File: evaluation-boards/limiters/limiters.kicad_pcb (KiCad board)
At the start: 4 copper layers, 180 x 20 mm, 132 parts, among them J1 Conn_01x02, J10 Conn_Coaxial, J11 Conn_Coaxial, J12 Conn_Coaxial, J13 Conn_Coaxial, J14 Conn_Coaxial, J15 Conn_Coaxial, J16 Conn_Coaxial, J17 Conn_Coaxial, J18 Conn_Coaxial, J19 Conn_Coaxial, J2 Conn_01x02, J20 Conn_Coaxial, J21 Conn_Coaxial, J22 Conn_Coaxial, J23 Conn_Coaxial, J24 Conn_Coaxial, J25 Conn_Coaxial, J26 Conn_Coaxial, J27 Conn_Coaxial, J28 Conn_Coaxial, J29 Conn_Coaxial, J3 Conn_Coaxial, J30 Conn_Coaxial, J31 Conn_Coaxial, J32 Conn_Coaxial, J33 Conn_Coaxial, J34 Conn_Coaxial, J35 Conn_Coaxial, J36 Conn_Coaxial, J37 Conn_Coaxial, J38 Conn_Coaxial, J4 Conn_Coaxial, J5 Conn_Coaxial, J6 Conn_Coaxial, J7 Conn_Coaxial, J8 Conn_Coaxial, J9 Conn_Coaxial, U1 SKY13453

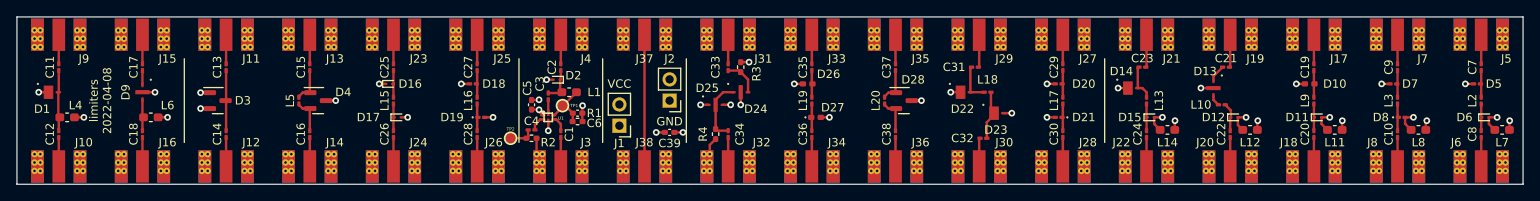
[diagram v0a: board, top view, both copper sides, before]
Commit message: Update RF test boards
- limiters
- rf-switch-spdt
- rf-switch-sp3t
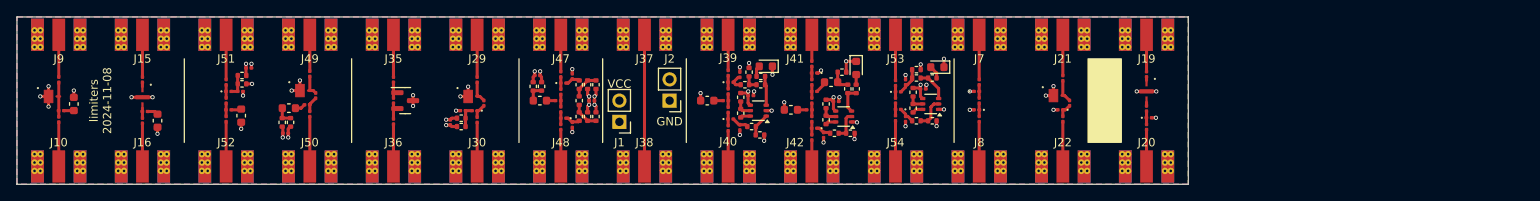
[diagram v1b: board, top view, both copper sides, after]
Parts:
- removed C14, C15, C16, C19, C20, C25, C26, C27, C28, C29, C30, C33, C34, C35, C36: 220 nF, Capacitor_SMD:C_0201_0603Metric_Pad0.64x0.40mm_HandSolder
- removed C39: 10 nF, Capacitor_SMD:C_0402_1005Metric_Pad0.74x0.62mm_HandSolder
- removed D10, D26, D27: D, Diode_SMD:D_0402_1005Metric_Pad0.77x0.64mm_HandSolder
- removed D11, D12, D15, D16, D17, D6: D_Schottky, Diode_SMD:D_SOD-923
- removed D18, D19: D_Schottky, Diode_SMD:D_0201_0603Metric_Pad0.64x0.40mm_HandSolder
- removed D20, D21: D, Diode_SMD:D_0201_0603Metric_Pad0.64x0.40mm_HandSolder
- removed D23: D, limiters:SMP1345-087LF
- removed D24, D25: D_AKA, limiters:SMP1304-085LF
- removed J11, J12, J13, J14, J17, J18, J23, J24, J25, J26, J27, J28, J3, J31, J32, J33, J34, J4, J5, J6: Conn_Coaxial, limiters:SMA-EDGE
- removed L11, L12, L14, L6, L7, L8: L, Inductor_SMD:L_0603_1608Metric_Pad1.05x0.95mm_HandSolder
- removed L15, L17, L19: 1.4 nH, Inductor_SMD:L_0201_0603Metric_Pad0.64x0.40mm_HandSolder
- removed L16: 1.0 nH, Inductor_SMD:L_0201_0603Metric_Pad0.64x0.40mm_HandSolder
- removed L9: 0.4 nH, Inductor_SMD:L_0201_0603Metric_Pad0.64x0.40mm_HandSolder
- removed R3, R4: 10k, Resistor_SMD:R_0402_1005Metric_Pad0.72x0.64mm_HandSolder
- removed TP1, TP2: TestPoint, gsg-modules:TESTPOINT-50MIL
- removed U1: SKY13453, gsg-modules:SKY13350-385LF
- added C40: 1 uF, Capacitor_SMD:C_0201_0603Metric, F.Cu at (130.0, 106.7)
- added C41: 1 uF, Capacitor_SMD:C_0201_0603Metric, F.Cu at (130.0, 113.3)
- added C42: 1 uF, Capacitor_SMD:C_0201_0603Metric, F.Cu at (131.4, 106.9)
- added C43: 1 uF, Capacitor_SMD:C_0201_0603Metric, F.Cu at (131.4, 113.2)
- added C44: 1 uF, Capacitor_SMD:C_0201_0603Metric, F.Cu at (140.0, 105.6)
- added C46: 1 uF, Capacitor_SMD:C_0201_0603Metric, F.Cu at (141.4, 114.1)
- added C47: 1 uF, Capacitor_SMD:C_0201_0603Metric, F.Cu at (140.0, 114.4)
- added C52: 1 uF, Capacitor_SMD:C_0201_0603Metric, F.Cu at (140.0, 110.0)
- added C63: 1 uF, Capacitor_SMD:C_0201_0603Metric, F.Cu at (110.0, 106.8)
- added C64: 1 uF, Capacitor_SMD:C_0201_0603Metric, F.Cu at (111.4, 107.1)
- added C65: 220 nF, Capacitor_SMD:C_0201_0603Metric, F.Cu at (80.0, 106.8)
- added C66: 220 nF, Capacitor_SMD:C_0201_0603Metric, F.Cu at (80.0, 111.6)
- added C67: 220 nF, Capacitor_SMD:C_0201_0603Metric, F.Cu at (70.0, 107.8)
- added C68: 1 uF, Capacitor_SMD:C_0201_0603Metric, F.Cu at (111.4, 112.9)
- added C69: 1 uF, Capacitor_SMD:C_0201_0603Metric, F.Cu at (110.0, 113.2)
- added C70: 220 nF, Capacitor_SMD:C_0201_0603Metric, F.Cu at (70.0, 112.2)
- added C71: 1 uF, Capacitor_SMD:C_0201_0603Metric, F.Cu at (71.7, 108.9)
- added C72: 1 uF, Capacitor_SMD:C_0201_0603Metric, F.Cu at (150.0, 107.9)
- added C73: 1 uF, Capacitor_SMD:C_0201_0603Metric, F.Cu at (151.2, 107.8)
- added C74: 1 uF, Capacitor_SMD:C_0201_0603Metric, F.Cu at (151.2, 112.2)
- added C75: 1 uF, Capacitor_SMD:C_0201_0603Metric, F.Cu at (150.0, 112.1)
- added D29: PIN, Diode_SMD:D_0201_0603Metric, F.Cu at (130.3, 107.8)
- added D30: Schottky, Diode_SMD:D_0201_0603Metric, F.Cu at (130.3, 112.2)
- added D31: PIN, Diode_SMD:D_0201_0603Metric, F.Cu at (140.3, 106.7)
- added D32: Schottky, Diode_SMD:D_0201_0603Metric, F.Cu at (140.3, 113.3)
- added D33: LED, LED_SMD:LED_0603_1608Metric, F.Cu at (134.5, 105.9)
- added D34: LED, LED_SMD:LED_0603_1608Metric, F.Cu at (145.3, 106.1)
- added D35: LED, LED_SMD:LED_0603_1608Metric, F.Cu at (155.0, 106.0)
- added D37: PIN, Diode_SMD:D_0201_0603Metric, F.Cu at (110.3, 107.9)
- added D38: Schottky, Diode_SMD:D_0201_0603Metric, F.Cu at (110.3, 112.1)
- added D39: PIN, limiters:SMP1345-087LF, F.Cu at (79.0, 108.8)
- added D41: PIN, Diode_SMD:D_0201_0603Metric, F.Cu at (150.3, 109.0)
- added D42: Schottky, Diode_SMD:D_0201_0603Metric, F.Cu at (150.3, 111.0)
- added J39: Conn_Coaxial, sma-variants:Linx_SMA_CONSMA003.062, F.Cu at (130.0, 100.0)
- added J40: Conn_Coaxial, sma-variants:Linx_SMA_CONSMA003.062, F.Cu at (130.0, 120.0)
- added J41: Conn_Coaxial, sma-variants:Linx_SMA_CONSMA003.062, F.Cu at (140.0, 100.0)
- added J42: Conn_Coaxial, sma-variants:Linx_SMA_CONSMA003.062, F.Cu at (140.0, 120.0)
- added J47: Conn_Coaxial, sma-variants:Linx_SMA_CONSMA003.062, F.Cu at (110.0, 100.0)
- added J48: Conn_Coaxial, sma-variants:Linx_SMA_CONSMA003.062, F.Cu at (110.0, 120.0)
- added J49: Conn_Coaxial, sma-variants:Linx_SMA_CONSMA003.062, F.Cu at (80.0, 100.0)
- added J50: Conn_Coaxial, sma-variants:Linx_SMA_CONSMA003.062, F.Cu at (80.0, 120.0)
- added J51: Conn_Coaxial, sma-variants:Linx_SMA_CONSMA003.062, F.Cu at (70.0, 100.0)
- added J52: Conn_Coaxial, sma-variants:Linx_SMA_CONSMA003.062, F.Cu at (70.0, 120.0)
- added J53: Conn_Coaxial, sma-variants:Linx_SMA_CONSMA003.062, F.Cu at (150.0, 100.0)
- added J54: Conn_Coaxial, sma-variants:Linx_SMA_CONSMA003.062, F.Cu at (150.0, 120.0)
- added L21: 0.5 nH, Inductor_SMD:L_0201_0603Metric, F.Cu at (130.0, 111.1)
- added L22: 47uH, Inductor_SMD:L_0603_1608Metric, F.Cu at (127.5, 110.0)
- added L23: 33nH, Inductor_SMD:L_0201_0603Metric, F.Cu at (129.7, 110.0)
- added L24: 0.5 nH, Inductor_SMD:L_0201_0603Metric, F.Cu at (130.0, 108.9)
- added L25: 0.5 nH, Inductor_SMD:L_0201_0603Metric, F.Cu at (140.0, 107.8)
- added L26: 47uH, Inductor_SMD:L_0603_1608Metric, F.Cu at (137.5, 111.1)
- added L27: 33nH, Inductor_SMD:L_0201_0603Metric, F.Cu at (139.7, 111.1)
- added L28: 0.5 nH, Inductor_SMD:L_0201_0603Metric, F.Cu at (140.0, 112.2)
- added L29: 47uH, Inductor_SMD:L_0603_1608Metric, F.Cu at (142.3, 107.8)
- added L30: 33nH, Inductor_SMD:L_0201_0603Metric, F.Cu at (140.3, 108.9)
- added L35: 0.5 nH, Inductor_SMD:L_0201_0603Metric, F.Cu at (110.0, 109.0)
- added L37: 47uH, Inductor_SMD:L_0603_1608Metric, F.Cu at (107.5, 110.0)
- added L38: 33nH, Inductor_SMD:L_0201_0603Metric, F.Cu at (109.7, 110.0)
- added L39: 0.5 nH, Inductor_SMD:L_0201_0603Metric, F.Cu at (110.0, 111.0)
- added L40: 0.5 nH, Inductor_SMD:L_0201_0603Metric, F.Cu at (70.0, 110.0)
- added L41: 47uH, Inductor_SMD:L_0603_1608Metric, F.Cu at (77.5, 110.9)
- added L42: 33nH, Inductor_SMD:L_0201_0603Metric, F.Cu at (79.7, 110.5)
- added L43: 0.5 nH, Inductor_SMD:L_0201_0603Metric, F.Cu at (80.7, 109.4)
- added L44: 47uH, Inductor_SMD:L_0603_1608Metric, F.Cu at (71.8, 111.8)
- added L45: 33nH, Inductor_SMD:L_0201_0603Metric, F.Cu at (70.3, 111.1)
- added L46: 1 nH, Inductor_SMD:L_0201_0603Metric, F.Cu at (150.0, 110.0)
- added Q1: NPN+PNP, Package_TO_SOT_SMD:SOT-363_SC-70-6, F.Cu at (133.6, 111.2)
- added Q2: NPN+PNP, Package_TO_SOT_SMD:SOT-363_SC-70-6, F.Cu at (143.8, 111.9)
- added Q3: NPN+PNP, Package_TO_SOT_SMD:SOT-363_SC-70-6, F.Cu at (154.2, 110.4)
- added R10: 1k, Resistor_SMD:R_0402_1005Metric, F.Cu at (133.9, 108.1)
- added R11: 0, Resistor_SMD:R_0402_1005Metric, F.Cu at (132.0, 108.1)
- added R12: 1k, Resistor_SMD:R_0402_1005Metric, F.Cu at (133.9, 107.1)
- added R13: 10k, Resistor_SMD:R_0402_1005Metric, F.Cu at (143.6, 106.6)
- added R14: 1k, Resistor_SMD:R_0402_1005Metric, F.Cu at (144.3, 108.6)
- added R15: 10k, Resistor_SMD:R_0402_1005Metric, F.Cu at (141.7, 110.4)
- added R16: 1k, Resistor_SMD:R_0402_1005Metric, F.Cu at (141.7, 112.3)
- added R17: 1k, Resistor_SMD:R_0402_1005Metric, F.Cu at (142.7, 113.9)
- added R18: 10k, Resistor_SMD:R_0402_1005Metric, F.Cu at (144.6, 113.9)
- added R19: 1k, Resistor_SMD:R_0402_1005Metric, F.Cu at (145.3, 108.6)
- added R20: 1k, Resistor_SMD:R_0402_1005Metric, F.Cu at (154.4, 107.3)
- added R36: 10k, Resistor_SMD:R_0402_1005Metric, F.Cu at (113.2, 111.9)
- added R37: 10k, Resistor_SMD:R_0402_1005Metric, F.Cu at (114.2, 111.9)
- added R38: 0, Resistor_SMD:R_0402_1005Metric, F.Cu at (112.2, 111.9)
- added R39: 0, Resistor_SMD:R_0402_1005Metric, F.Cu at (112.2, 108.1)
- added R40: 1k, Resistor_SMD:R_0402_1005Metric, F.Cu at (76.7, 112.6)
- added R41: 10k, Resistor_SMD:R_0402_1005Metric, F.Cu at (77.7, 112.6)
- added R42: 1k, Resistor_SMD:R_0402_1005Metric, F.Cu at (71.9, 108.0)
- added R43: 10k, Resistor_SMD:R_0402_1005Metric, F.Cu at (71.9, 107.0)
- added R44: 1k, Resistor_SMD:R_0402_1005Metric, F.Cu at (106.7, 108.3)
- added R45: 10k, Resistor_SMD:R_0402_1005Metric, F.Cu at (107.7, 108.3)
- added R46: 10k, Resistor_SMD:R_0402_1005Metric, F.Cu at (114.2, 108.1)
- added R47: 10k, Resistor_SMD:R_0402_1005Metric, F.Cu at (113.2, 108.1)
- added R48: 0, Resistor_SMD:R_0402_1005Metric, F.Cu at (112.2, 110.0)
- added R49: 1k, Resistor_SMD:R_0402_1005Metric, F.Cu at (152.5, 106.3)
- added R5: 10k, Resistor_SMD:R_0402_1005Metric, F.Cu at (133.8, 114.1)
- added R50: 3.3k, Resistor_SMD:R_0402_1005Metric, F.Cu at (152.5, 107.3)
- added R51: 10k, Resistor_SMD:R_0402_1005Metric, F.Cu at (152.1, 109.0)
- added R52: 1k, Resistor_SMD:R_0402_1005Metric, F.Cu at (152.1, 110.9)
- added R53: 1k, Resistor_SMD:R_0402_1005Metric, F.Cu at (152.5, 112.4)
- added R54: 10k, Resistor_SMD:R_0402_1005Metric, F.Cu at (154.4, 112.4)
- added R6: 10k, Resistor_SMD:R_0402_1005Metric, F.Cu at (131.5, 109.6)
- added R7: 1k, Resistor_SMD:R_0402_1005Metric, F.Cu at (132.8, 113.1)
- added R8: 1k, Resistor_SMD:R_0402_1005Metric, F.Cu at (131.5, 111.5)
- added R9: 10k, Resistor_SMD:R_0402_1005Metric, F.Cu at (132.5, 106.6)
- C1, C13, C2, C3, C4, C7, C8: value 220 nF -> 1 uF; footprint Capacitor_SMD:C_0201_0603Metric_Pad0.64x0.40mm_HandSolder -> Capacitor_SMD:C_0201_0603Metric
- C10, C11, C12, C17, C18, C21, C22, C23, C24, C31, C32, C37, C38, C9: footprint Capacitor_SMD:C_0201_0603Metric_Pad0.64x0.40mm_HandSolder -> Capacitor_SMD:C_0201_0603Metric
- C5: value 10 nF -> 1 uF; footprint Capacitor_SMD:C_0402_1005Metric_Pad0.74x0.62mm_HandSolder -> Capacitor_SMD:C_0201_0603Metric
- C6: value C -> 1 uF; footprint Capacitor_SMD:C_0402_1005Metric_Pad0.74x0.62mm_HandSolder -> Capacitor_SMD:C_0201_0603Metric
- D1, D14, D22: value D -> PIN
- D13, D9: value D_AKA -> PIN
- D2: value D_Schottky -> Schottky; footprint Diode_SMD:D_SOD-923 -> Diode_SMD:D_0201_0603Metric
- D28: value D_Dual_Series_AKC -> Dual_PIN
- D3: value D_Schottky_Dual_Series_AKC -> Schottky; footprint Package_TO_SOT_SMD:SOT-23 -> Diode_SMD:D_0201_0603Metric
- D4: value D_Schottky_Dual_Series_AKC -> PIN; footprint Package_TO_SOT_SMD:SOT-23 -> Diode_SMD:D_0201_0603Metric
- D5, D7: value D -> PIN; footprint Diode_SMD:D_0201_0603Metric_Pad0.64x0.40mm_HandSolder -> Diode_SMD:D_0201_0603Metric
- D8: value D_Schottky -> Schottky; footprint Diode_SMD:D_0201_0603Metric_Pad0.64x0.40mm_HandSolder -> Diode_SMD:D_0201_0603Metric
- J10, J15, J16, J19, J20, J21, J22, J29, J30, J35, J36, J37, J38, J7, J8, J9: footprint limiters:SMA-EDGE -> sma-variants:Linx_SMA_CONSMA003.062
- L1, L4: value L -> 33nH; footprint Inductor_SMD:L_0603_1608Metric_Pad1.05x0.95mm_HandSolder -> Inductor_SMD:L_0201_0603Metric
- L10, L18, L20, L3: footprint Inductor_SMD:L_0201_0603Metric_Pad0.64x0.40mm_HandSolder -> Inductor_SMD:L_0201_0603Metric
- L13: value 0.4 nH -> 0.5 nH; footprint Inductor_SMD:L_0201_0603Metric_Pad0.64x0.40mm_HandSolder -> Inductor_SMD:L_0201_0603Metric
- L2: value 0.4 nH -> 47uH; footprint Inductor_SMD:L_0201_0603Metric_Pad0.64x0.40mm_HandSolder -> Inductor_SMD:L_0603_1608Metric
- L5: value 1.4 nH -> 47uH; footprint Inductor_SMD:L_0201_0603Metric_Pad0.64x0.40mm_HandSolder -> Inductor_SMD:L_0603_1608Metric
- R1: value 10k -> 1k; footprint Resistor_SMD:R_0402_1005Metric_Pad0.72x0.64mm_HandSolder -> Resistor_SMD:R_0402_1005Metric
- R2: value 50 -> 10k; footprint Resistor_SMD:R_0402_1005Metric_Pad0.72x0.64mm_HandSolder -> Resistor_SMD:R_0402_1005Metric
- moved L2 168.2 mm to (51.8, 110.4)
- moved D5 149.2 mm to (70.3, 108.9)
- moved D3 100.7 mm to (169.7, 111.1), turned to 180 degrees
- moved C7 87.4 mm to (132.7, 109.4), turned to 0 degrees
- moved C8 77.2 mm to (142.9, 110.1), turned to 0 degrees
- moved D2 70.9 mm to (180.3, 112.0), turned to 0 degrees
- moved L1 60.7 mm to (50.3, 111.2), turned to 0 degrees
- moved C32 60.5 mm to (100.0, 112.3), turned to 90 degrees
- moved L18 60.2 mm to (100.8, 110.3), turned to 90 degrees
- moved C37 60.0 mm to (90.0, 107.5)
- moved C38 60.0 mm to (90.0, 112.5)
- moved J29 60.0 mm to (100.0, 100.0)
- moved J30 60.0 mm to (100.0, 120.0)
- moved J35 60.0 mm to (90.0, 100.0)
- moved J36 60.0 mm to (90.0, 120.0)
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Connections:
- C1 pad 1: Net-(C1-Pad1) -> Net-(D4-A)
- C1 pad 2: Net-(C1-Pad2) -> GND
- C11 pad 1: Net-(C11-Pad1) -> Net-(D1-A)
- C12 pad 2: Net-(C11-Pad1) -> Net-(D1-A)
- C13 pad 1: Net-(C13-Pad1) -> VCC
- C13 pad 2: Net-(C13-Pad2) -> GND
- C2 pad 1: Net-(C2-Pad1) -> VCC
- C2 pad 2: Net-(C2-Pad2) -> GND
- C22 pad 2: Net-(C22-Pad2) -> Net-(D2-K)
- C24 pad 2: Net-(C24-Pad2) -> Net-(D3-K)
- C3 pad 1: Net-(C3-Pad1) -> VCC
- C3 pad 2: Net-(C2-Pad1) -> GND
- C32 pad 2: Net-(C32-Pad2) -> Net-(D4-K)
- C4 pad 1: Net-(C4-Pad1) -> VCC
- C4 pad 2: Net-(C4-Pad2) -> GND
- C5 pad 1: GND -> VCC
- C5 pad 2: VCC -> GND
- C6 pad 1: Net-(C6-Pad1) -> VCC
- C7 pad 1: Net-(C7-Pad1) -> VCC
- C7 pad 2: Net-(C7-Pad2) -> GND
- C8 pad 1: Net-(C8-Pad1) -> VCC
- C8 pad 2: Net-(C8-Pad2) -> GND
- D1 pad 2: Net-(C11-Pad1) -> Net-(D1-A)
- D2 pad 1: Net-(C2-Pad1) -> Net-(D2-K)
- D3 pad 1: GND -> Net-(D3-K)
- D4 pad 1: Net-(C15-Pad1) -> Net-(D4-K)
- D4 pad 2: Net-(C16-Pad2) -> Net-(D4-A)
- D5 pad 1: GND -> Net-(D5-K)
- D5 pad 2: Net-(C7-Pad1) -> Net-(D5-A)
- L1 pad 1: Net-(C6-Pad1) -> Net-(D1-A)
- L1 pad 2: Net-(C2-Pad1) -> Net-(L1-Pad2)
- L10 pad 1: Net-(C22-Pad2) -> Net-(D2-K)
- L13 pad 1: Net-(C24-Pad2) -> Net-(D3-K)
- L18 pad 1: Net-(C32-Pad2) -> Net-(D4-K)
- L2 pad 1: Net-(C8-Pad2) -> Net-(L1-Pad2)
- L2 pad 2: Net-(C7-Pad1) -> GND
- L4 pad 1: Net-(C11-Pad1) -> Net-(C18-Pad2)
- L4 pad 2: GND -> Net-(L4-Pad2)
- L5 pad 1: Net-(C16-Pad2) -> Net-(L4-Pad2)
- L5 pad 2: Net-(C15-Pad1) -> GND
- R1 pad 1: Net-(C6-Pad1) -> Net-(D4-A)
- R2 pad 1: Net-(C4-Pad1) -> Net-(D4-A)
- R2 pad 2: GND -> VCC
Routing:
- net VCC: track 5.31 -> 16.7 mm, vias 4 -> 9
- net GND: track 55.6 -> 47.1 mm, vias 40 -> 55
- net Net-(C34-Pad2): track 7.58 -> 0.00 mm
- net Net-(C11-Pad1): track 7.33 -> 0.00 mm
- net Net-(C13-Pad1): track 7.19 -> 0.00 mm
- net Net-(C6-Pad1): track 6.58 -> 0.00 mm
- net Net-(C32-Pad2): track 6.01 -> 0.00 mm
- net Net-(J50-In): track 0.00 -> 5.95 mm
- net Net-(J54-In): track 0.00 -> 5.45 mm
- net Net-(J53-In): track 0.00 -> 5.45 mm
- net Net-(J52-In): track 0.00 -> 5.35 mm
- net Net-(J51-In): track 0.00 -> 5.35 mm
- net Net-(J48-In): track 0.00 -> 4.40 mm
- net Net-(J47-In): track 0.00 -> 4.40 mm
- net Net-(C2-Pad1): track 4.37 -> 0.00 mm
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- added copper zone on B.Cu, net GND
- added copper zone on F.Cu, net GND
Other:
- board size 180 x 20 mm -> 140 x 20 mm
- board text added: "limiters 2024-11-08"
- board text removed: "limiters 2022-04-08"

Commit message: Update limiters board
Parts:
- removed C37, C38, C65, C66: 220 nF, Capacitor_SMD:C_0201_0603Metric
- removed C40, C41, C42, C43, C44, C46, C47, C52, C72, C73, C74, C75: 1 uF, Capacitor_SMD:C_0201_0603Metric
- removed D22, D39: PIN, limiters:SMP1345-087LF
- removed D28: Dual_PIN, Package_TO_SOT_SMD:SOT-23
- removed D29, D31, D41: PIN, Diode_SMD:D_0201_0603Metric
- removed D30, D32, D42: Schottky, Diode_SMD:D_0201_0603Metric
- removed D33, D34, D35: LED, LED_SMD:LED_0603_1608Metric
- removed J20, J21, J22, J29, J30, J35, J36, J39, J40, J41, J42, J49, J50, J53, J54: Conn_Coaxial, sma-variants:Linx_SMA_CONSMA003.062
- removed L10: 0.6 nH, Inductor_SMD:L_0201_0603Metric
- removed L13, L21, L24, L25, L28, L35, L39, L40, L43: 0.5 nH, Inductor_SMD:L_0201_0603Metric
- removed L18: 0.8 nH, Inductor_SMD:L_0201_0603Metric
- removed L20: 1.4 nH, Inductor_SMD:L_0201_0603Metric
- removed L22, L26, L29, L37, L41, L44: 47uH, Inductor_SMD:L_0603_1608Metric
- removed L23, L27, L30, L38, L42, L45: 33nH, Inductor_SMD:L_0201_0603Metric
- removed L46: 1 nH, Inductor_SMD:L_0201_0603Metric
- removed Q3: NPN+PNP, Package_TO_SOT_SMD:SOT-363_SC-70-6
- removed R18, R45, R51, R54: 10k, Resistor_SMD:R_0402_1005Metric
- removed R19, R20, R44, R49, R52, R53: 1k, Resistor_SMD:R_0402_1005Metric
- removed R50: 3.3k, Resistor_SMD:R_0402_1005Metric
- added C14: C, Capacitor_SMD:C_0201_0603Metric, F.Cu at (87.2, 109.5)
- added C15: 1 uF, Capacitor_SMD:C_0201_0603Metric, F.Cu at (138.4, 111.2)
- added C16: 1 uF, Capacitor_SMD:C_0402_1005Metric, F.Cu at (100.0, 108.6)
- added C19: 1 uF, Capacitor_SMD:C_0201_0603Metric, F.Cu at (130.0, 113.0)
- added C20: 1 uF, Capacitor_SMD:C_0201_0603Metric, F.Cu at (128.6, 110.7)
- added C25: C, Capacitor_SMD:C_0201_0603Metric, F.Cu at (122.9, 108.6)
- added C26: C, Capacitor_SMD:C_0201_0603Metric, F.Cu at (125.3, 106.4)
- added C27: 1 uF, Capacitor_SMD:C_0201_0603Metric, F.Cu at (126.7, 106.4)
- added C28: 1 uF, Capacitor_SMD:C_0201_0603Metric, F.Cu at (122.9, 107.2)
- added C29: 1 uF, Capacitor_SMD:C_0201_0603Metric, F.Cu at (148.3, 111.0)
- added C30: 1 uF, Capacitor_SMD:C_0201_0603Metric, F.Cu at (150.0, 110.6)
- added C33: 1 uF, Capacitor_SMD:C_0201_0603Metric, F.Cu at (160.0, 110.7)
- added C34: 1 uF, Capacitor_SMD:C_0201_0603Metric, F.Cu at (143.7, 113.4)
- added C35: 1 uF, Capacitor_SMD:C_0201_0603Metric, F.Cu at (153.8, 113.4)
- added D10: PIN, eval:TSLP-2-19, F.Cu at (148.9, 109.5)
- added D11: Schottky, eval:TSSLP-2-1, F.Cu at (149.2, 110.2)
- added D12: PIN, eval:TSLP-2-19, F.Cu at (158.9, 109.1)
- added D6: Schottky, eval:TSSLP-2-1, F.Cu at (100.8, 109.8)
- added J11: Conn_Coaxial, sma-variants:Linx_SMA_CONSMA003.062, F.Cu at (100.0, 120.0)
- added J12: Conn_Coaxial, sma-variants:Linx_SMA_CONSMA003.062, F.Cu at (130.0, 100.0)
- added J13: Conn_Coaxial, sma-variants:Linx_SMA_CONSMA003.062, F.Cu at (130.0, 120.0)
- added J14: Conn_Coaxial, sma-variants:Linx_SMA_CONSMA003.062, F.Cu at (150.0, 100.0)
- added J17: Conn_Coaxial, sma-variants:Linx_SMA_CONSMA003.062, F.Cu at (160.0, 100.0)
- added J18: Conn_Coaxial, sma-variants:Linx_SMA_CONSMA003.062, F.Cu at (160.0, 120.0)
- added J3: Conn_Coaxial, sma-variants:Linx_SMA_CONSMA003.062, F.Cu at (110.0, 100.0)
- added J4: Conn_Coaxial, sma-variants:Linx_SMA_CONSMA003.062, F.Cu at (110.0, 120.0)
- added J5: Conn_Coaxial, sma-variants:Linx_SMA_CONSMA003.062, F.Cu at (140.0, 100.0)
- added J6: Conn_Coaxial, sma-variants:Linx_SMA_CONSMA003.062, F.Cu at (140.0, 120.0)
- added L6: 1.0 nH, Inductor_SMD:L_0201_0603Metric, F.Cu at (130.0, 110.0)
- added L7: L, Inductor_SMD:L_0805_2012Metric, F.Cu at (76.9, 111.2)
- added L8: L, Inductor_SMD:L_0201_0603Metric, F.Cu at (78.3, 110.0)
- added L9: L, Inductor_SMD:L_0201_0603Metric, F.Cu at (79.7, 110.0)
- added Q4: NMOS/PMOS, Package_TO_SOT_SMD:SOT-563, F.Cu at (134.6, 111.7)
- added R21: R, Resistor_SMD:R_0201_0603Metric, F.Cu at (86.8, 110.6)
- added R22: R, Resistor_SMD:R_0201_0603Metric, F.Cu at (87.2, 108.2)
- added R23: 10k, Resistor_SMD:R_0402_1005Metric, F.Cu at (135.1, 109.8)
- added R24: 10k, Resistor_SMD:R_0402_1005Metric, F.Cu at (136.7, 113.1)
- added R25: 10k, Resistor_SMD:R_0402_1005Metric, F.Cu at (127.7, 110.9)
- added R27: 10k, Resistor_SMD:R_0402_1005Metric, F.Cu at (128.0, 106.6)
- added R28: 10k, Resistor_SMD:R_0402_1005Metric, F.Cu at (125.9, 114.2)
- added R29: 10k, Resistor_SMD:R_0402_1005Metric, F.Cu at (126.9, 114.2)
- added R3: R, Resistor_SMD:R_0201_0603Metric, F.Cu at (86.5, 109.5)
- added R30: 10k, Resistor_SMD:R_0402_1005Metric, F.Cu at (122.3, 112.6)
- added R31: 10k, Resistor_SMD:R_0402_1005Metric, F.Cu at (122.0, 108.4)
- added R32: 10k, Resistor_SMD:R_0402_1005Metric, F.Cu at (124.1, 114.2)
- added R33: 3.3k, Resistor_SMD:R_0402_1005Metric, F.Cu at (122.3, 114.2)
- added R34: 10k, Resistor_SMD:R_0402_1005Metric, F.Cu at (121.3, 114.2)
- added R35: 0, Resistor_SMD:R_0402_1005Metric, F.Cu at (122.3, 110.8)
- added R4: R, Resistor_SMD:R_0201_0603Metric, F.Cu at (88.2, 109.9)
- added R55: 10k, Resistor_SMD:R_0402_1005Metric, F.Cu at (122.3, 109.8)
- added R56: 10k, Resistor_SMD:R_0402_1005Metric, F.Cu at (127.3, 108.5)
- added R57: 10k, Resistor_SMD:R_0402_1005Metric, F.Cu at (125.8, 105.1)
- added R58: 3.3k, Resistor_SMD:R_0402_1005Metric, F.Cu at (124.8, 105.1)
- added U1: MADL-011021-14150T, eval:TDFN-6-1EP_1.5x1.2mm_P0.4mm_EP0.47x0.8mm, F.Cu at (110.0, 110.0)
- added U2: LMV358, Package_SO:MSOP-8_3x3mm_P0.65mm, F.Cu at (125.0, 110.0)
- C10, C12, C17, C18, C21, C24, C32, C67, C70: value 220 nF -> 1 uF
- C11, C22, C23: value 220 nF -> C
- C31, C9: value 220 nF -> 1 uF; footprint Capacitor_SMD:C_0201_0603Metric -> Capacitor_SMD:C_0402_1005Metric
- C4, C8: footprint Capacitor_SMD:C_0201_0603Metric -> Capacitor_SMD:C_0402_1005Metric
- C6, C7: value 1 uF -> C
- D1, D14: footprint limiters:SMP1345-087LF -> eval:TSLP-2-19
- D13, D9: value PIN -> Schottky; footprint limiters:SMP1304-085LF -> eval:TSSLP-2-1
- D2, D38, D8: footprint Diode_SMD:D_0201_0603Metric -> eval:TSSLP-2-1
- D3: value Schottky -> PIN; footprint Diode_SMD:D_0201_0603Metric -> eval:TSLP-2-19
- D37, D4, D5, D7: footprint Diode_SMD:D_0201_0603Metric -> eval:TSLP-2-19
- J16, J19, J9: value Conn_Coaxial -> Conn_01x02; footprint sma-variants:Linx_SMA_CONSMA003.062 -> Connector_PinHeader_2.54mm:PinHeader_1x02_P2.54mm_Vertical
- L1: value 33nH -> L
- L2: value 47uH -> L; footprint Inductor_SMD:L_0603_1608Metric -> Inductor_SMD:L_0201_0603Metric
- L4: value 33nH -> L; footprint Inductor_SMD:L_0201_0603Metric -> Inductor_SMD:L_0805_2012Metric
- L5: value 47uH -> 1.0 nH; footprint Inductor_SMD:L_0603_1608Metric -> Inductor_SMD:L_0201_0603Metric
- Q1, Q2: value NPN+PNP -> NMOS/PMOS; footprint Package_TO_SOT_SMD:SOT-363_SC-70-6 -> Package_TO_SOT_SMD:SOT-563
- R12, R16, R40: value 1k -> 10k
- R15, R2, R41: value 10k -> 0
- R17, R7, R8: value 1k -> R; footprint Resistor_SMD:R_0402_1005Metric -> Resistor_SMD:R_0201_0603Metric
- R42: value 1k -> 0
- R5, R6: value 10k -> R; footprint Resistor_SMD:R_0402_1005Metric -> Resistor_SMD:R_0201_0603Metric
- moved J15 92.2 mm to (150.0, 120.0), turned to 90 degrees
- moved D7 90.7 mm to (69.0, 109.8)
- moved D8 90.5 mm to (69.2, 110.5)
- moved C9 90.0 mm to (70.0, 108.4)
- moved C12 90.0 mm to (140.0, 111.4)
- moved C10 90.0 mm to (70.0, 111.4)
- moved D1 90.0 mm to (139.0, 109.8), turned to 180 degrees
- moved J7 90.0 mm to (70.0, 100.0)
- moved J8 90.0 mm to (70.0, 120.0)
- moved L3 90.0 mm to (70.0, 110.0)
- moved J16 86.7 mm to (145.8, 107.5), turned to -90 degrees
- moved J9 86.6 mm to (136.3, 107.5)
- moved L5 78.2 mm to (140.0, 110.0), turned to 90 degrees
- moved C6 76.1 mm to (77.2, 109.0), turned to -90 degrees
- moved C18 70.2 mm to (130.0, 107.0)
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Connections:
- C1 pad 1: Net-(D4-A) -> Net-(U1-RFIN)
- C1 pad 2: GND -> Net-(J3-In)
- C11 pad 1: Net-(D1-A) -> GND
- C11 pad 2: Net-(J9-In) -> Net-(C11-Pad2)
- C12 pad 1: Net-(J10-In) -> Net-(J6-In)
- C12 pad 2: Net-(D1-A) -> Net-(D2-A)
- C17 pad 1: Net-(C17-Pad1) -> Net-(J11-In)
- C17 pad 2: Net-(J15-In) -> Net-(D4-A)
- C18 pad 1: Net-(J16-In) -> Net-(D3-K)
- C18 pad 2: Net-(C18-Pad2) -> Net-(J12-In)
- C21 pad 1: Net-(C21-Pad1) -> Net-(D3-A)
- C21 pad 2: Net-(J19-In) -> GND
- C22 pad 1: Net-(J20-In) -> Net-(C22-Pad1)
- C22 pad 2: Net-(D2-K) -> Net-(U2A--)
- C23 pad 1: Net-(D14-A) -> Net-(C22-Pad1)
- C23 pad 2: Net-(J21-In) -> Net-(U2A-+)
- C24 pad 1: Net-(J22-In) -> Net-(U2A-+)
- C24 pad 2: Net-(D3-K) -> GND
- C3 pad 1: VCC -> Net-(J4-In)
- C3 pad 2: GND -> Net-(U1-RFOUT)
- C31 pad 1: Net-(D22-A) -> Net-(D12-K)
- C32 pad 1: Net-(J30-In) -> Net-(D13-K)
- C32 pad 2: Net-(D4-K) -> GND
- C4 pad 1: VCC -> Net-(D1-K)
- C4 pad 2: GND -> Net-(J5-In)
- C6 pad 1: VCC -> Net-(C6-Pad1)
- C6 pad 2: GND -> Net-(C6-Pad2)
- C67 pad 1: Net-(D5-K) -> Net-(D5-A)
- C69 pad 2: Net-(D38-A) -> Net-(D37-K)
- C7 pad 1: VCC -> GND
- C7 pad 2: GND -> Net-(C7-Pad2)
- C70 pad 2: Net-(C70-Pad2) -> Net-(D5-A)
- C71 pad 1: Net-(D5-A) -> Net-(D5-K)
- C8 pad 1: VCC -> Net-(D10-K)
- C8 pad 2: GND -> Net-(J14-In)
- D1 pad 1: GND -> Net-(D1-K)
- D1 pad 2: Net-(D1-A) -> GND
- D13 pad 1: Net-(C21-Pad1) -> Net-(D13-K)
- D13 pad 2: GND -> Net-(D12-K)
- D14 pad 2: Net-(D14-A) -> Net-(D12-K)
- D2 pad 2: GND -> Net-(D2-A)
- D3 pad 2: GND -> Net-(D3-A)
- D38 pad 2: Net-(D38-A) -> Net-(D37-K)
- D4 pad 1: Net-(D4-K) -> GND
- D9 pad 1: Net-(C17-Pad1) -> Net-(D9-K)
- D9 pad 2: GND -> Net-(D9-A)
- J16 pad 1: Net-(J16-In) -> Net-(J16-Pin_1)
- J16 pad 2: GND -> Net-(J16-Pin_1)
- J19 pad 1: Net-(J19-In) -> Net-(J19-Pin_1)
- J19 pad 2: GND -> Net-(J19-Pin_1)
- J9 pad 1: Net-(J9-In) -> Net-(J9-Pin_1)
- J9 pad 2: GND -> Net-(J9-Pin_1)
- L1 pad 1: Net-(D1-A) -> Net-(D5-A)
- L2 pad 2: GND -> Net-(C14-Pad2)
- L4 pad 1: Net-(C18-Pad2) -> Net-(C14-Pad2)
- L5 pad 1: Net-(L4-Pad2) -> Net-(D2-A)
- L5 pad 2: GND -> Net-(D1-K)
- Q1 pad 1: Net-(Q1A-E1) -> GND
- Q1 pad 2: GND -> Net-(J16-Pin_1)
- Q1 pad 3: Net-(Q1B-C2) -> Net-(Q1B-D)
- Q1 pad 5: Net-(Q1B-B2) -> Net-(J16-Pin_1)
- Q1 pad 6: Net-(Q1A-C1) -> Net-(Q1A-D)
- Q2 pad 2: Net-(Q2A-B1) -> Net-(J19-Pin_1)
- Q2 pad 5: Net-(Q2B-B2) -> Net-(J19-Pin_1)
- Q2 pad 6: Net-(Q2A-C1) -> Net-(Q2A-D)
- R1 pad 1: Net-(D4-A) -> Net-(D2-K)
- R1 pad 2: GND -> Net-(Q4B-D)
- R10 pad 1: Net-(R10-Pad1) -> Net-(D11-K)
- R10 pad 2: Net-(Q1B-C2) -> Net-(Q1B-D)
- R11 pad 1: Net-(D29-A) -> Net-(D11-K)
- R11 pad 2: Net-(R10-Pad1) -> Net-(Q1A-D)
- R12 pad 1: Net-(D33-A) -> Net-(J16-Pin_1)
- R12 pad 2: Net-(Q1B-C2) -> GND
- R13 pad 1: Net-(L29-Pad2) -> Net-(D13-K)
- R14 pad 1: Net-(L29-Pad2) -> Net-(D13-K)
- R15 pad 1: VCC -> Net-(D13-K)
- R15 pad 2: Net-(Q2B-B2) -> Net-(Q2A-D)
- R16 pad 1: Net-(Q2B-B2) -> Net-(J19-Pin_1)
- R16 pad 2: Net-(Q2A-C1) -> GND
- R17 pad 1: Net-(D32-K) -> Net-(L4-Pad2)
- R17 pad 2: Net-(Q2A-B1) -> VCC
- R2 pad 1: Net-(D4-A) -> Net-(D2-K)
- R2 pad 2: VCC -> Net-(Q4A-D)
- R40 pad 1: Net-(L41-Pad2) -> Net-(D3-A)
- R40 pad 2: GND -> Net-(U2B-+)
- R41 pad 1: Net-(L41-Pad2) -> Net-(U2B--)
- R41 pad 2: VCC -> GND
- R42 pad 1: Net-(D5-A) -> Net-(D5-K)
- R43 pad 1: Net-(D5-A) -> Net-(D5-K)
- R5 pad 1: Net-(Q1A-E1) -> Net-(C6-Pad2)
- R5 pad 2: GND -> VCC
- R6 pad 1: VCC -> Net-(L8-Pad1)
- R6 pad 2: Net-(Q1B-B2) -> Net-(C6-Pad2)
- R7 pad 1: Net-(D30-A) -> VCC
- R7 pad 2: Net-(Q1A-E1) -> Net-(C7-Pad2)
- R8 pad 1: Net-(Q1B-B2) -> Net-(C6-Pad1)
- R8 pad 2: Net-(Q1A-C1) -> GND
- R9 pad 1: Net-(R10-Pad1) -> Net-(D11-K)
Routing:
- net Net-(D3-A): track 0.00 -> 16.7 mm
- net Net-(C22-Pad1): track 0.00 -> 13.5 mm
- net Net-(J19-Pin_1): track 0.00 -> 10.5 mm
- net Net-(J16-Pin_1): track 0.00 -> 10.4 mm
- net Net-(J9-Pin_1): track 0.00 -> 10.3 mm
- net Net-(U2A-+): track 0.00 -> 9.41 mm
- net Net-(U2A--): track 0.00 -> 8.37 mm
- net Net-(J11-In): track 0.00 -> 7.34 mm
- net Net-(J18-In): track 0.00 -> 6.84 mm
- net GND: track 47.1 -> 40.3 mm, vias 55 -> 50
- net Net-(U2B-+): track 0.00 -> 6.56 mm
- net Net-(D9-K): track 0.00 -> 6.46 mm
- net Net-(U2B--): track 0.00 -> 6.41 mm
- net Net-(J14-In): track 0.00 -> 6.38 mm
- net Net-(J6-In): track 0.00 -> 6.15 mm
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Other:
- board size 140 x 20 mm -> 100 x 20 mm
- board text added: "limiters 2024-12-09"
- board text removed: "limiters 2024-11-08"
